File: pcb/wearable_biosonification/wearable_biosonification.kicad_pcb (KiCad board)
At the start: 2 copper layers, 23.5 x 51 mm, 16 parts, among them J1 Electrodes, J2 1.5V, U1 LM324

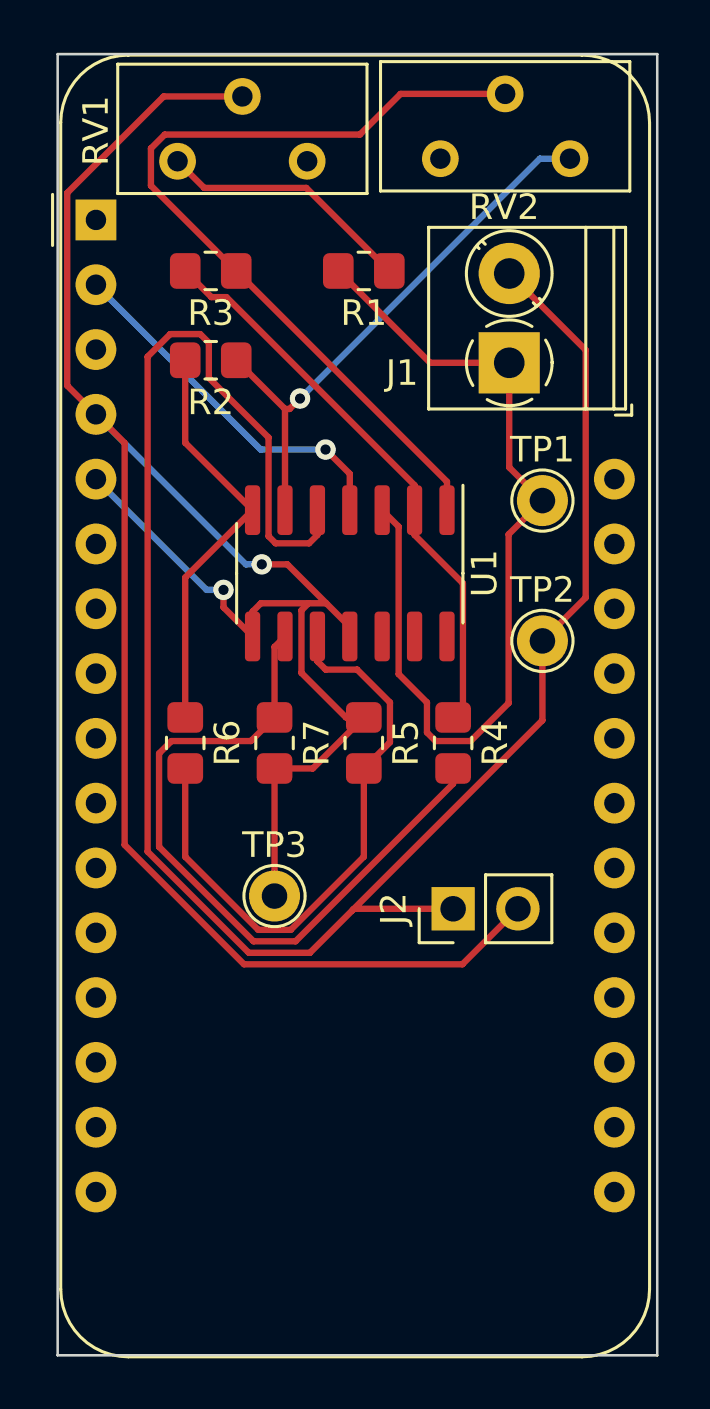
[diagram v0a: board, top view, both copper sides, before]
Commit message: removed testpoints + added LED
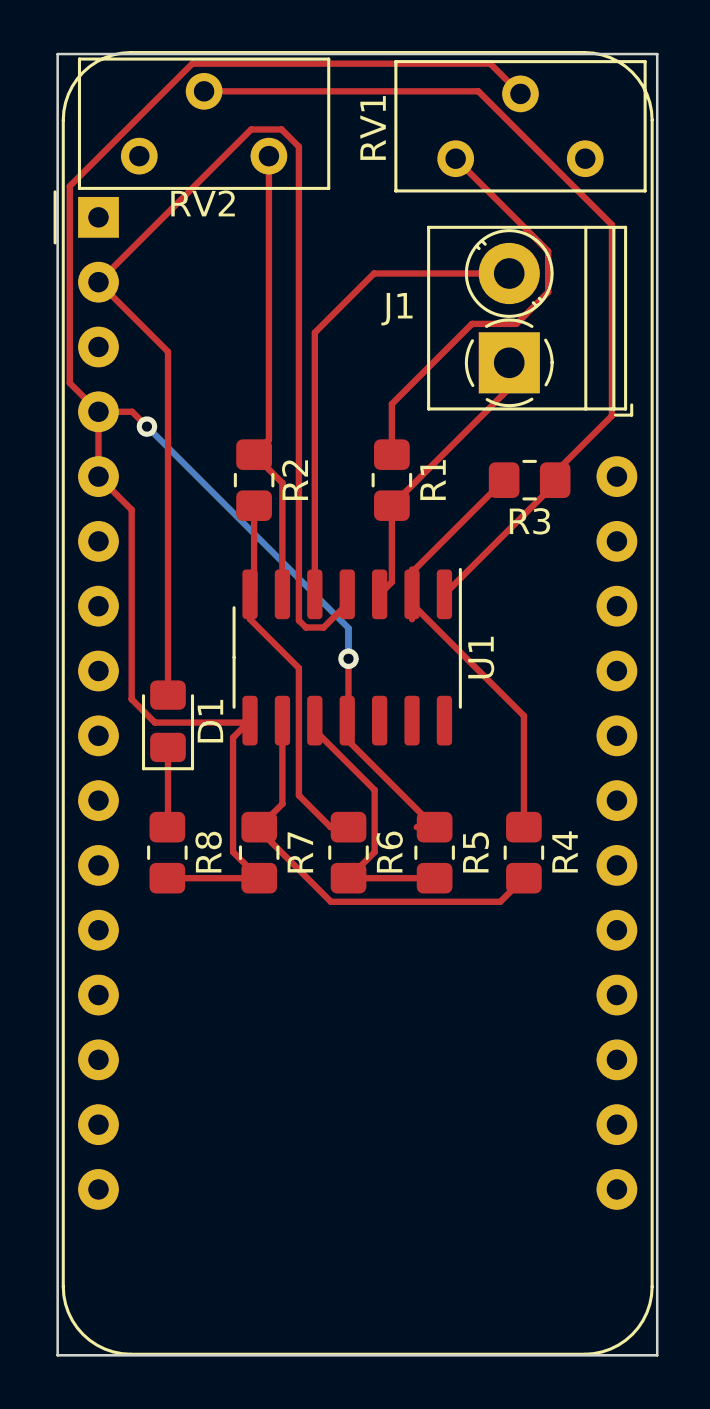
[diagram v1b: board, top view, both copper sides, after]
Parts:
- removed J2: 1.5V, Connector_PinHeader_2.54mm:PinHeader_1x02_P2.54mm_Vertical
- removed TP1, TP2, TP3: Out, TestPoint:TestPoint_THTPad_D2.0mm_Drill1.0mm
- added D1: LED, LED_SMD:LED_0805_2012Metric_Pad1.15x1.40mm_HandSolder, F.Cu at (72.3, 78.7)
- added R8: 1k, Resistor_SMD:R_0805_2012Metric_Pad1.20x1.40mm_HandSolder, F.Cu at (72.3, 83.8)
- moved R3 14.9 mm to (86.5, 69.2)
- moved RV2 11.8 mm to (71.2, 56.5)
- moved RV1 10.9 mm to (83.6, 56.6)
- moved R1 8.27 mm to (81.1, 69.2), turned to 270 degrees
- moved R6 7.71 mm to (79.4, 83.8)
- moved R4 5.12 mm to (86.3, 83.8)
- moved R5 5.12 mm to (82.8, 83.8)
- moved R2 5.00 mm to (75.7, 69.2), turned to 270 degrees
- moved R7 4.34 mm to (75.9, 83.8)
- moved U1 3.30 mm to (79.3, 76.2)
- moved A1 0.14 mm to (69.6, 58.9)
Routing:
- net Net-(J1-Pad2): track 78.3 -> 18.8 mm
- net Vfeather: track 14.4 -> 49.3 mm, vias 1 -> 0
- net Net-(J1-Pad1): track 36.8 -> 12.0 mm
- net AnalogIn: track 95.4 -> 80.4 mm
- net Net-(R5-Pad2): track 23.8 -> 10.9 mm
- net Net-(R4-Pad2): track 28.3 -> 16.6 mm
- net Net-(R1-Pad1): track 10.1 -> 16.7 mm
- net Net-(R2-Pad1): track 21.9 -> 17.9 mm, vias 1 -> 0
- net Net-(D1-Pad1): track 0.00 -> 3.14 mm
- net Net-(R3-Pad2): track 22.5 -> 19.4 mm
- net Net-(R3-Pad1): track 33.8 -> 35.4 mm
- net Net-(R2-Pad2): track 16.2 -> 14.7 mm
